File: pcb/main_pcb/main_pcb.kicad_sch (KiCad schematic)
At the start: 14 parts

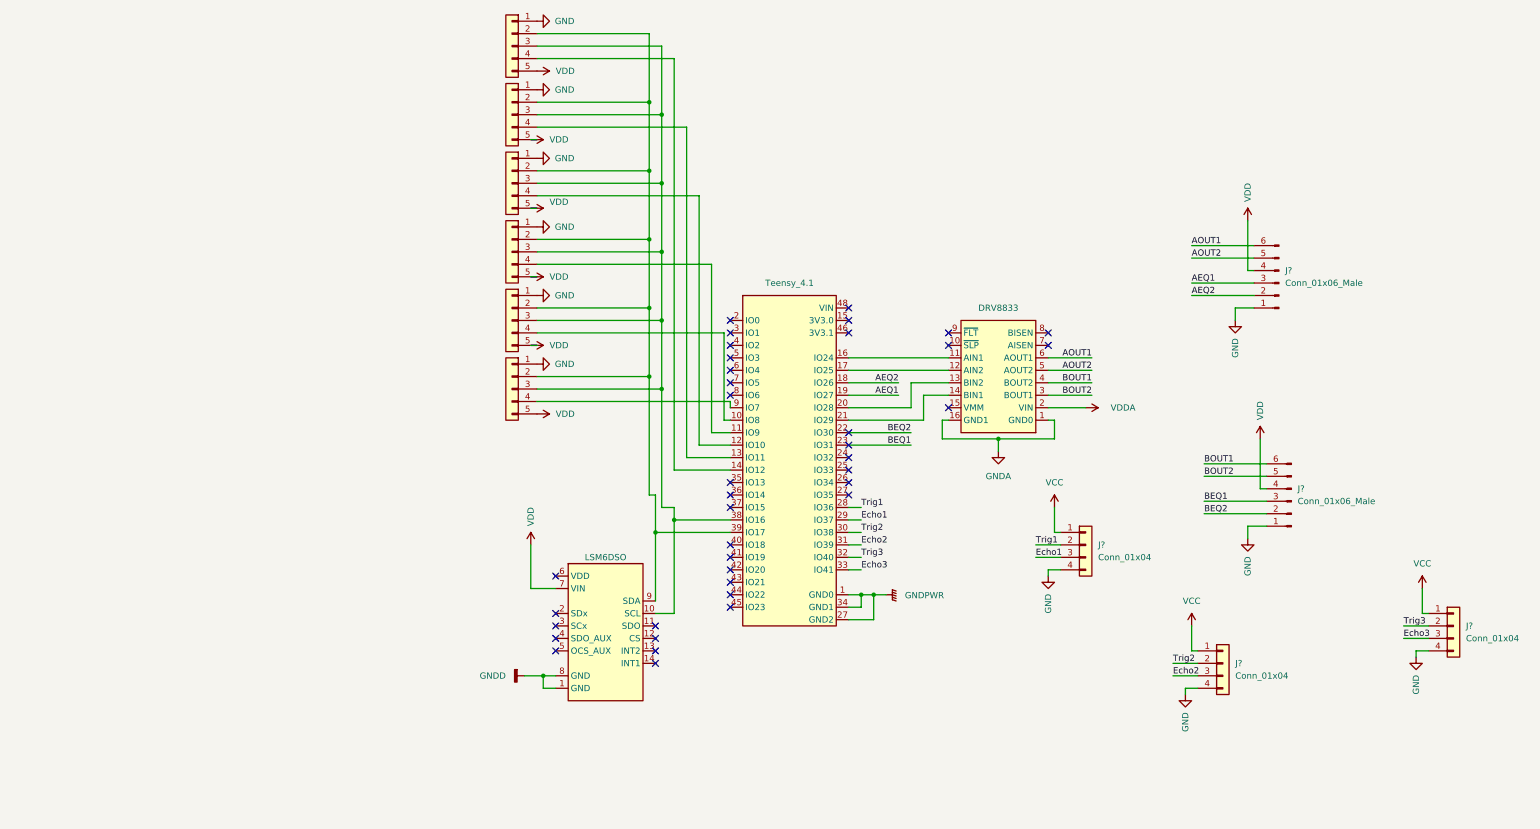
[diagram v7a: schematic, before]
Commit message: Add power regulators to schematic
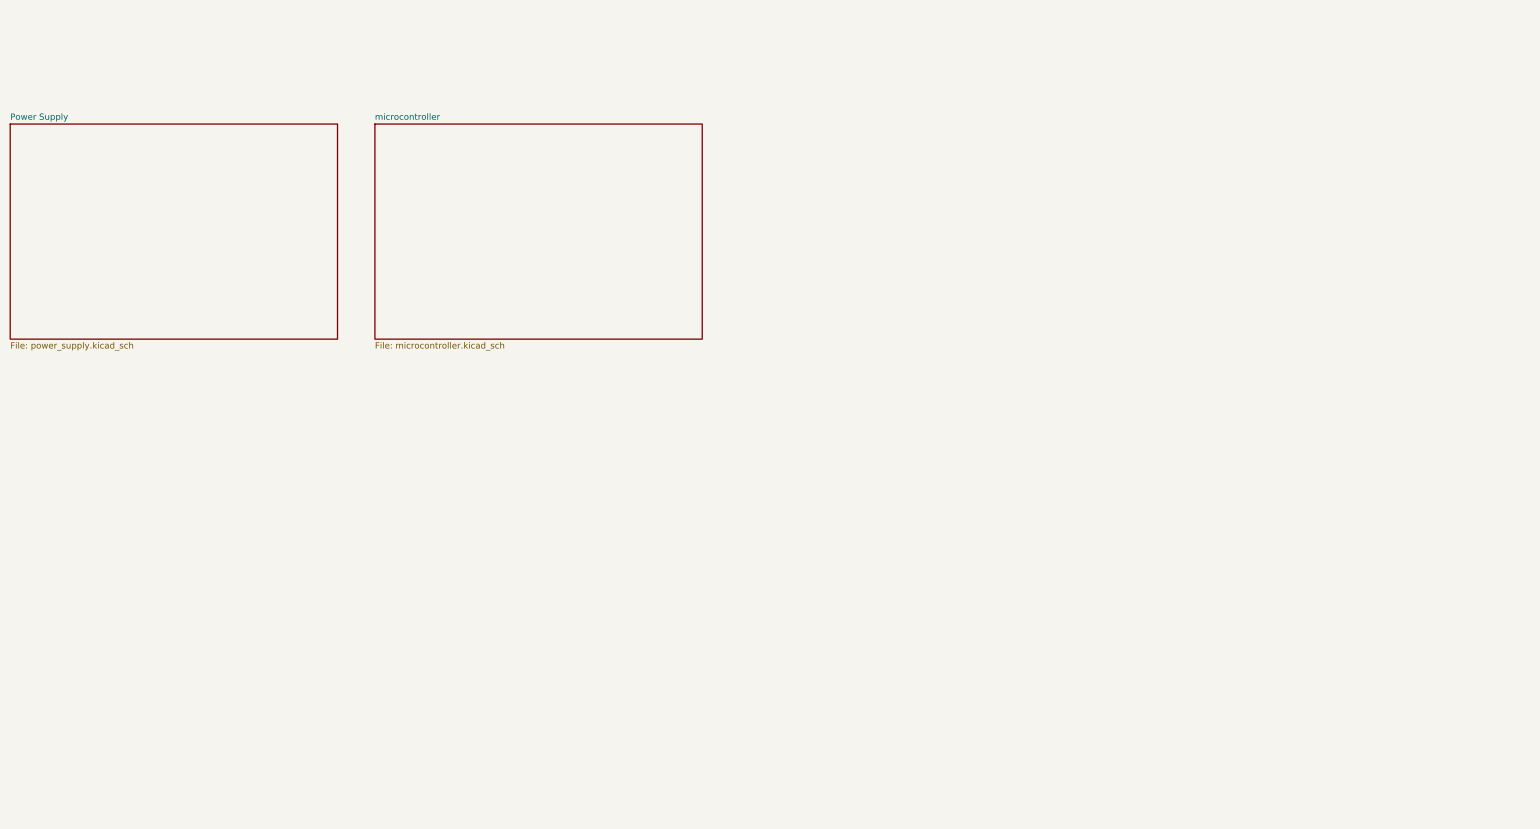
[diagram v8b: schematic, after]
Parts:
- removed J? (x6): Conn_01x04, symbol Connector_Generic:Conn_01x05
- removed J? (x3): Conn_01x04, symbol Connector_Generic:Conn_01x04
- removed J? (x2): Conn_01x06_Male, symbol Connector:Conn_01x06_Male
- removed U?: DRV8833, symbol sym_library:DRV8833
- removed U?: Teensy_4.1, symbol sym_library:Teensy_4.1
- removed U?: LSM6DSO, symbol sym_library:LSM6DSO
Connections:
- no-connect marks 39 -> 0
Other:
- added sheet Power Supply (power_supply.kicad_sch)
- added sheet microcontroller (microcontroller.kicad_sch)
